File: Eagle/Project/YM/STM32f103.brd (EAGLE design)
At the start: 174.2 x 90.3 mm, 81 parts, among them IC1 YM3812, IC10 YM3812, IC11 YM3014B, IC12 LM358N, IC13 BA033CC0T, IC14 74ALS04N, IC15 6N136, IC2 YM3014B, IC3 LM358N, IC4 YM3812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

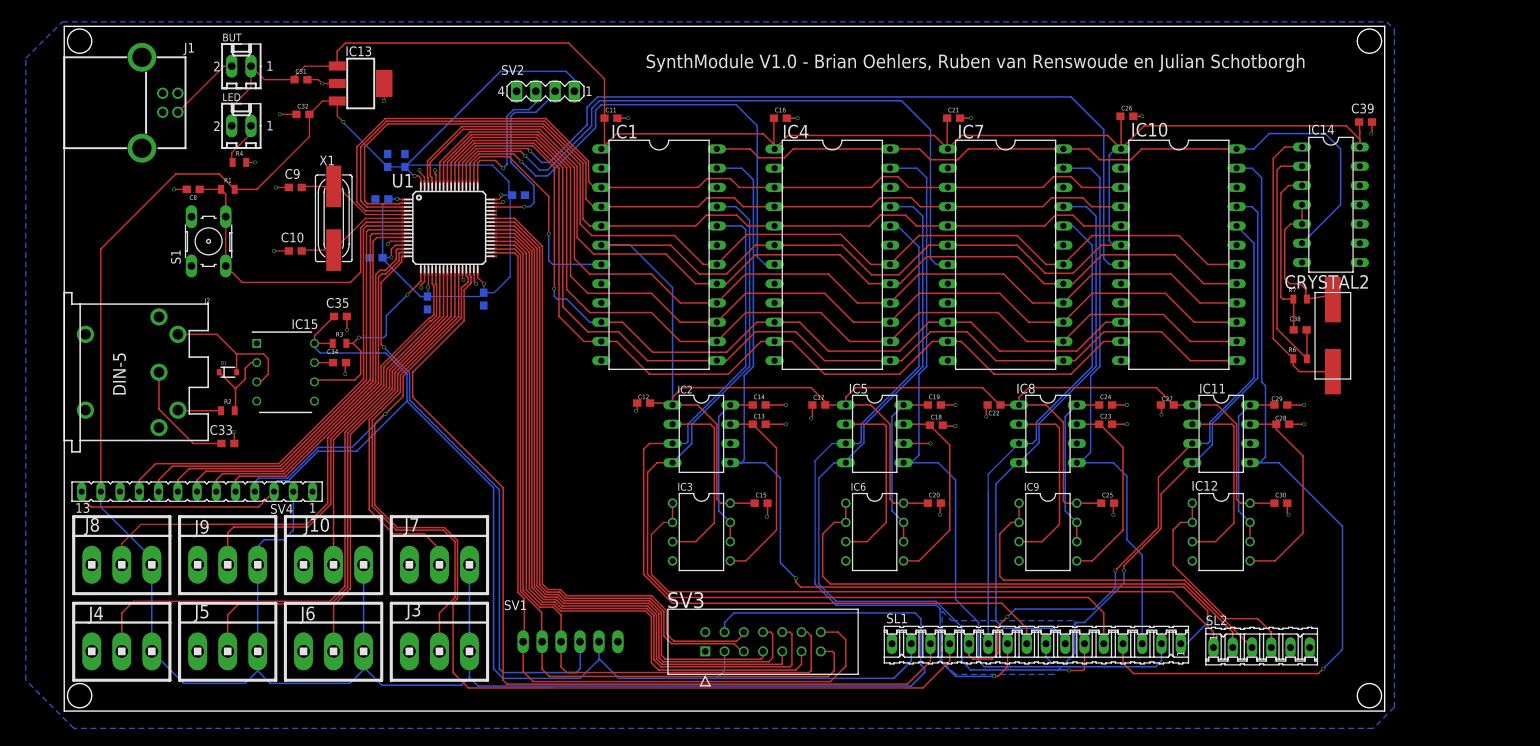
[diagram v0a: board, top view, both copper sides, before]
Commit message: PCB V5.0 LDO Adjustment
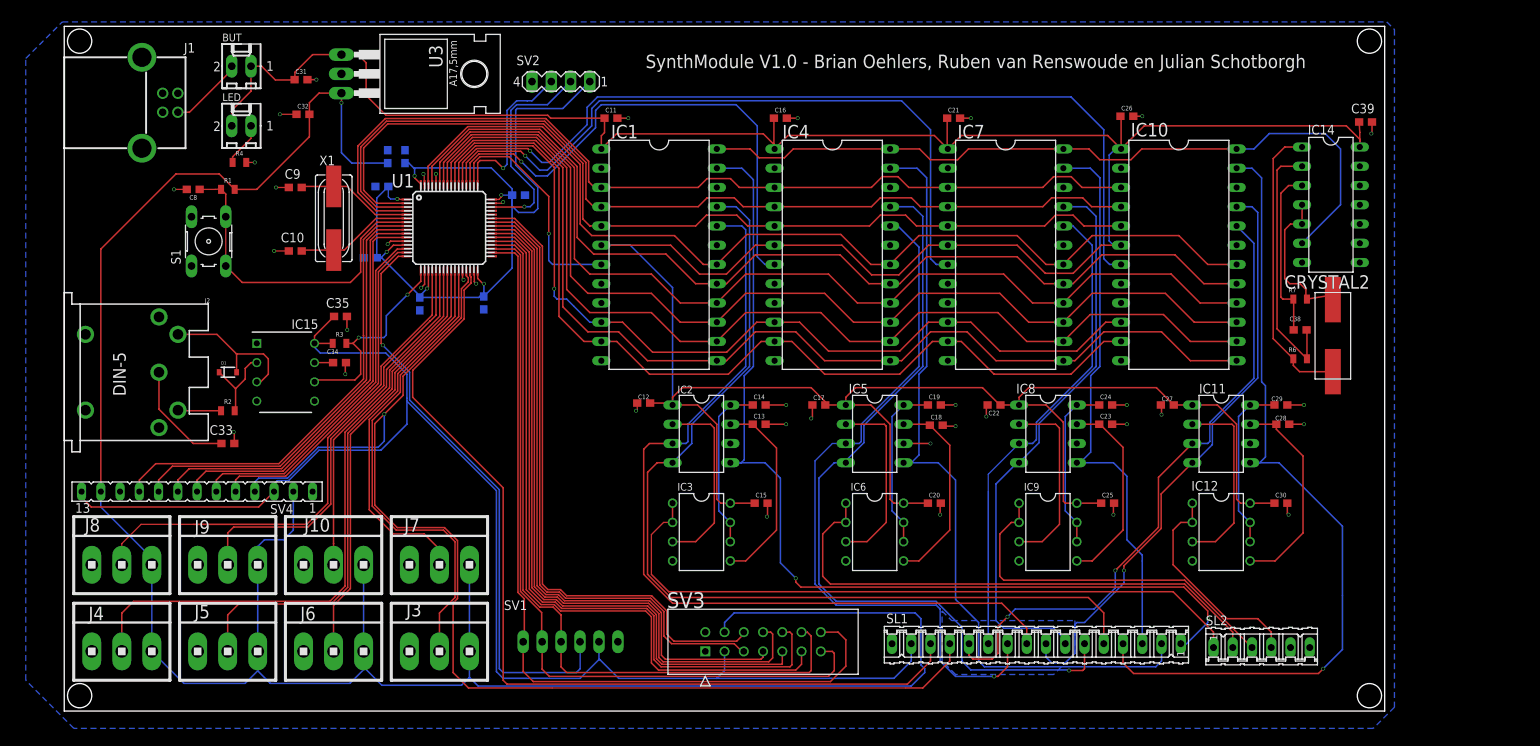
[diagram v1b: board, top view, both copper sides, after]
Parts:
- removed IC13: BA033CC0T, LDO:SOT223
- added U3: (no value), bt_regulator:TO220BH
- moved SV2 2.40 mm to (65.5, 83.1)
- moved C2 1.65 mm to (41.9, 69.2)
- moved C3 1.02 mm to (46.9, 53.7)
- moved C4 0.76 mm to (40.4, 59.8)
- moved C5 0.51 mm to (55.3, 53.8)
- moved C1 0.51 mm to (42.7, 73.2)
- moved C7 0.51 mm to (45.0, 73.2)
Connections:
- net 3.3V: now also U3.3; no longer IC13.3
- net 5V: now also U3.1; no longer IC13.1
- net GND: now also U3.2; no longer IC13.2, IC13.4
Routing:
- net 3.3V: track 417.2 -> 425.9 mm
- net GND: track 73.7 -> 67.3 mm, vias 39 -> 38
- net SW-DIO: track 25.8 -> 28.6 mm
- net SW-CLK: track 19.9 -> 22.0 mm
- net USART-TX-M4: track 159.1 -> 160.9 mm
- net YM-RST: track 125.3 -> 124.4 mm
- net RST: track 44.6 -> 43.8 mm
- net IO1: track 62.2 -> 61.4 mm
- net YM-A0: track 125.6 -> 124.8 mm
- net YM-WR: track 127.3 -> 126.6 mm
- net IO2: track 59.3 -> 58.6 mm
- net YM-D6: track 134.5 -> 133.8 mm
- net YM-D7: track 133.5 -> 133.0 mm

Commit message: V5.1 Connectors edit
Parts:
- removed SL1: (no value), con-amp-quick:16P
- removed SL2: (no value), con-amp-quick:06P
- added SV5: (no value), con-lsta:FE13
- added SV6: (no value), con-lsta:FE06
- moved R4 3.49 mm to (26.5, 73.0)
- moved J1 3.43 mm to (7.75, 76.8)
- moved C35 1.15 mm to (36.3, 50.9)
- moved C13 0.38 mm to (92.1, 37.8)
- moved U3 0.38 mm to (42.9, 84.5)
- moved C23 0.25 mm to (137.7, 37.8)
- moved C24 0.25 mm to (137.7, 40.4)
- moved C14 0.25 mm to (91.9, 40.4)
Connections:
- net 5V: now also SV5.12; no longer SL1.15
- net DAC-OUT-0: now also SV6.1; no longer SL2.1
- net DAC-OUT-1: now also SV6.2; no longer SL2.2
- net DAC-OUT-2: now also SV6.3; no longer SL2.3
- net DAC-OUT-3: now also SV6.4; no longer SL2.4
- net GND: now also SV5.13, SV6.6; no longer SL1.16, SL2.6
- net USART-RX-M4: now also SV5.11; no longer SL1.14
- net USART-TX-M4: now also SV5.10; no longer SL1.13
- net YM-CLK-I: now also SV5.1
- net YM1-CLK-O: no longer SL1.1
- net YM1-OUTPUT: now also SV5.2; no longer SL1.5
- net YM1-SYNC: now also SV5.6; no longer SL1.9
- net YM2-CLK-O: no longer SL1.2
- net YM2-OUTPUT: now also SV5.3; no longer SL1.6
- net YM2-SYNC: now also SV5.7; no longer SL1.10
- net YM3-CLK-O: no longer SL1.3
- net YM3-OUTPUT: now also SV5.4; no longer SL1.7
- net YM3-SYNC: now also SV5.8; no longer SL1.11
- net YM4-CLK-O: no longer SL1.4
- net YM4-OUTPUT: now also SV5.5; no longer SL1.8
- net YM4-SYNC: now also SV5.9; no longer SL1.12
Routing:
- net YM-CLK-I: track 101.9 -> 191.3 mm
- net YM1-CLK-O: track 129.1 -> 44.5 mm, vias 2 -> 0
- net YM4-CLK-O: track 108.5 -> 43.2 mm, vias 1 -> 0
- net YM2-CLK-O: track 104.8 -> 44.8 mm
- net 5V: track 664.9 -> 698.3 mm
- net YM3-CLK-O: track 74.7 -> 44.5 mm
- net YM4-OUTPUT: track 78.4 -> 84.3 mm, vias 1 -> 0
- net 3.3V: track 425.9 -> 421.3 mm
- net ADC-VOL3: track 56.6 -> 60.9 mm
- net 5VBUTTON: track 9.94 -> 14.2 mm
- net GND: track 67.3 -> 64.4 mm
- net YM4-SYNC: track 84.5 -> 86.5 mm, vias 2 -> 1
- net YM3-OUTPUT: track 74.5 -> 76.4 mm
- net DAC-OUT-1: track 71.0 -> 69.7 mm
- net N$13: track 5.99 -> 4.77 mm
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
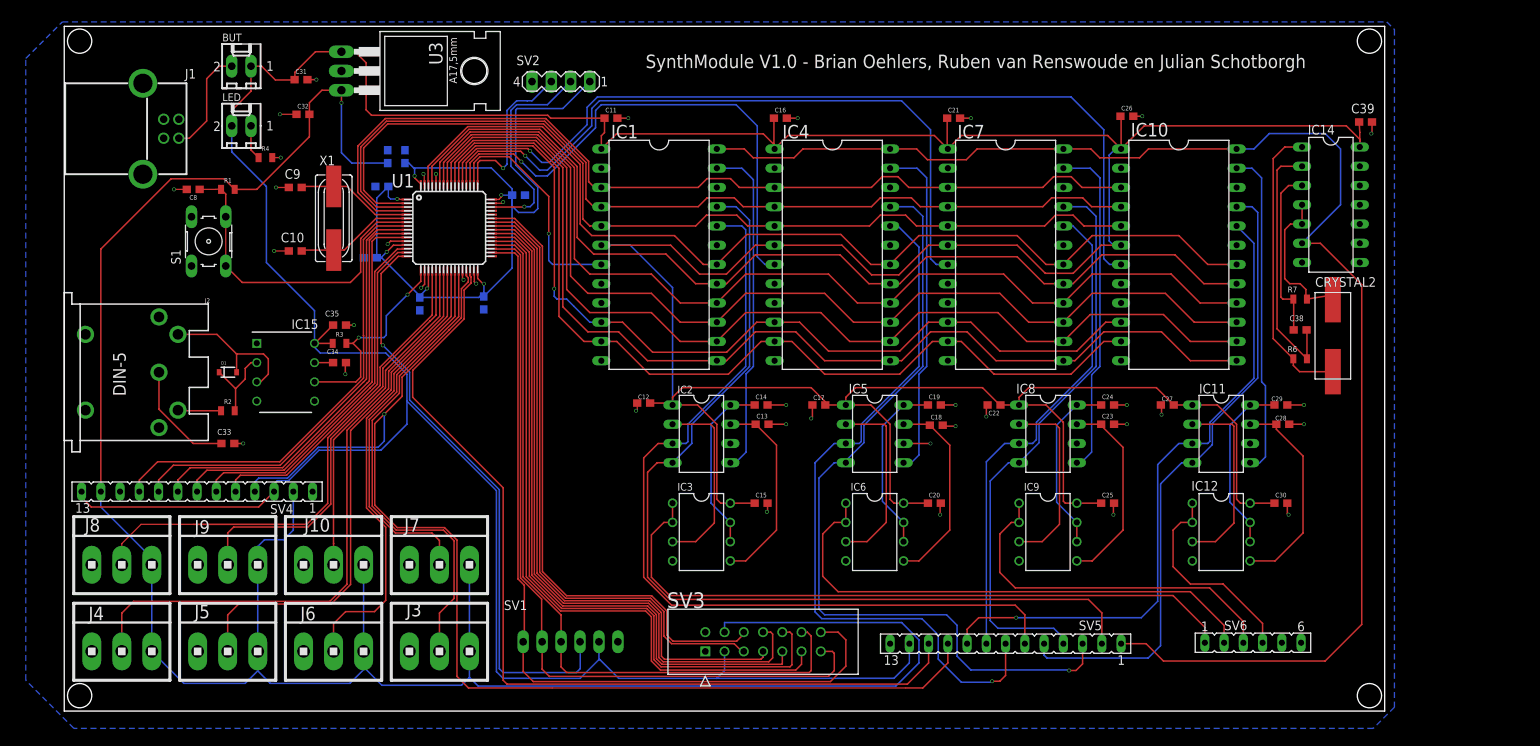
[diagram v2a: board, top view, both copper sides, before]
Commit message: Nieuwe versie - aanpassing aan: componenten, ground, namen van componenten, usb verschoven
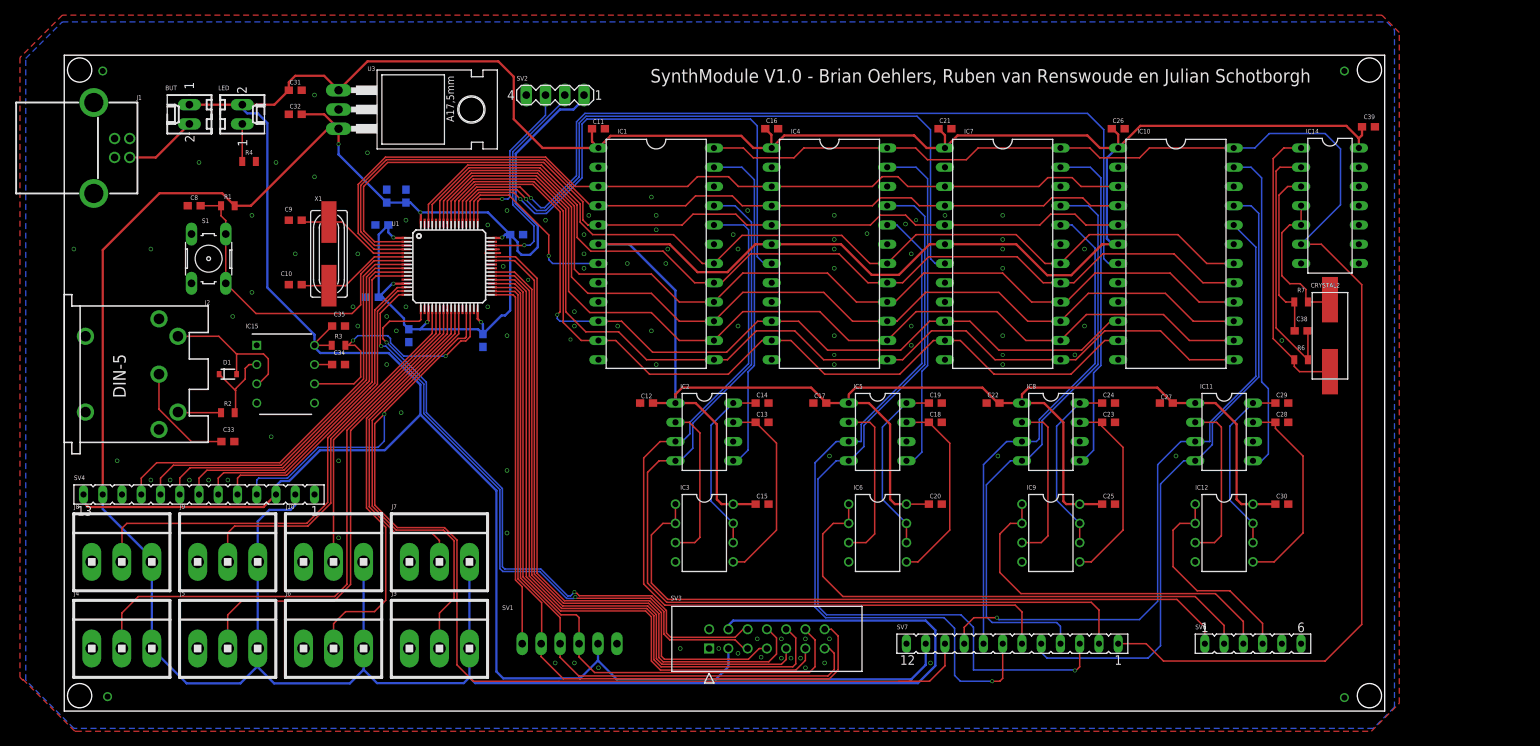
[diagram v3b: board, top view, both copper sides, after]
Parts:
- removed SV5: (no value), con-lsta:FE13
- added SV7: (no value), con-lsta:FE12
- C1, C2, C3, C5, C6: value 10nF -> 10n
- C10, C9: value 20pF -> 20p
- C11, C12, C15, C16, C17, C20, C21, C22, C25, C26, C27, C30, C8: value 100N -> 100n
- C13, C14, C18, C19, C23, C24, C28, C29: value 10UF -> 10u
- C31: value 0.47UF -> 0.47u
- C32: value 22UF -> 22u
- C33, C35, C39: value 100nF -> 100n
- C34: value 1p5F -> 1p5
- C38: value 4.7nF -> 4.7n
- C4: value 1uF -> 1u
- C7: value 4.7uF -> 4.7u
- IC12, IC3, IC6, IC9: value LM358N -> OPA2134
- moved BUT 9.35 mm to (16.5, 78.7), turned to 90 degrees
- moved J1 6.96 mm to (1.27, 74.3)
- moved C4 5.21 mm to (40.6, 54.6)
- moved C6 5.21 mm to (59.7, 62.9)
- moved C1 5.21 mm to (42.5, 67.9)
- moved C7 5.21 mm to (45.1, 67.9)
- moved U3 5.09 mm to (42.5, 79.4)
- moved C2 5.08 mm to (41.9, 64.1)
- moved U1 5.08 mm to (50.8, 58.7)
- moved C5 4.95 mm to (55.2, 48.9)
- moved X1 4.74 mm to (34.9, 60.3)
- moved C10 4.45 mm to (30.5, 56.3)
- moved C3 4.43 mm to (45.5, 49.5)
- moved C9 4.32 mm to (30.5, 64.8)
- moved S1 2.29 mm to (19.1, 59.7)
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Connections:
- removed net EXP1-INTA: SV3.8, U1.40
- removed net EXP1-INTB: SV3.7, U1.41
- removed net EXP2-INTA: SV3.5, U1.42
- removed net EXP2-INTB: SV3.6, U1.43
- removed net USART-RX-M4: SV5.11, U1.30
- new net EXP1-INT-A: SV3.8, U1.42
- new net EXP1-INT-B: SV3.7, U1.43
- new net EXP2-INT-A: SV3.5, U1.16
- new net EXP2-INT-B: SV3.6, U1.17
- net 5V: now also SV7.11; no longer SV5.12
- net EXP-SPI-CLK: now also SV1.2; no longer SV1.1
- net EXP-SPI-MISO: now also SV1.3; no longer SV1.2
- net EXP-SPI-MOSI: now also SV1.4; no longer SV1.3
- net GND: now also SV7.12, U1.40, U1.41, U1.44, U1.45; no longer SV5.13
- net LCD-SPI-CS: now also SV1.1, U1.33; no longer SV1.4, U1.16
- net USART-RX-MIDI: now also U1.30; no longer U1.17
- net USART-TX-M4: now also SV7.10; no longer SV5.10
- net YM-CLK-I: now also SV7.1; no longer SV5.1
- net YM1-OUTPUT: now also SV7.2; no longer SV5.2
- net YM1-SYNC: now also SV7.6; no longer SV5.6
- net YM2-OUTPUT: now also SV7.3; no longer SV5.3
- net YM2-SYNC: now also SV7.7; no longer SV5.7
- net YM3-OUTPUT: now also SV7.4; no longer SV5.4
- net YM3-SYNC: now also SV7.8; no longer SV5.8
- net YM4-OUTPUT: now also SV7.5; no longer SV5.5
- net YM4-SYNC: now also SV7.9; no longer SV5.9
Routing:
- net USART-RX-M4: track 122.2 -> 0.00 mm
- net EXP1-INTA: track 93.8 -> 0.00 mm
- net EXP1-INT-A: track 0.00 -> 89.8 mm
- net EXP1-INTB: track 88.7 -> 0.00 mm
- net EXP1-INT-B: track 0.00 -> 85.0 mm
- net EXP2-INT-A: track 0.00 -> 84.0 mm, vias 0 -> 2
- net EXP2-INTB: track 83.9 -> 0.00 mm
- net EXP2-INT-B: track 0.00 -> 83.7 mm, vias 0 -> 2
- net EXP2-INTA: track 83.6 -> 0.00 mm
- net GND: track 64.4 -> 6.10 mm, vias 38 -> 107
- net LCD-SPI-CS: track 77.5 -> 49.3 mm, vias 1 -> 0
- net EXP-SPI-CLK: track 109.9 -> 100.2 mm
- net USART-RX-MIDI: track 27.3 -> 35.3 mm
- net EXP-SPI-MISO: track 103.3 -> 95.4 mm
- net USART-TX-M4: track 160.3 -> 154.0 mm
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- added copper zone on layer 1, net GND
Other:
- board size 174.2 x 90.3 mm -> 174.2 x 86.5 mm

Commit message: verandere jumpers en verplaatsen din en usb.
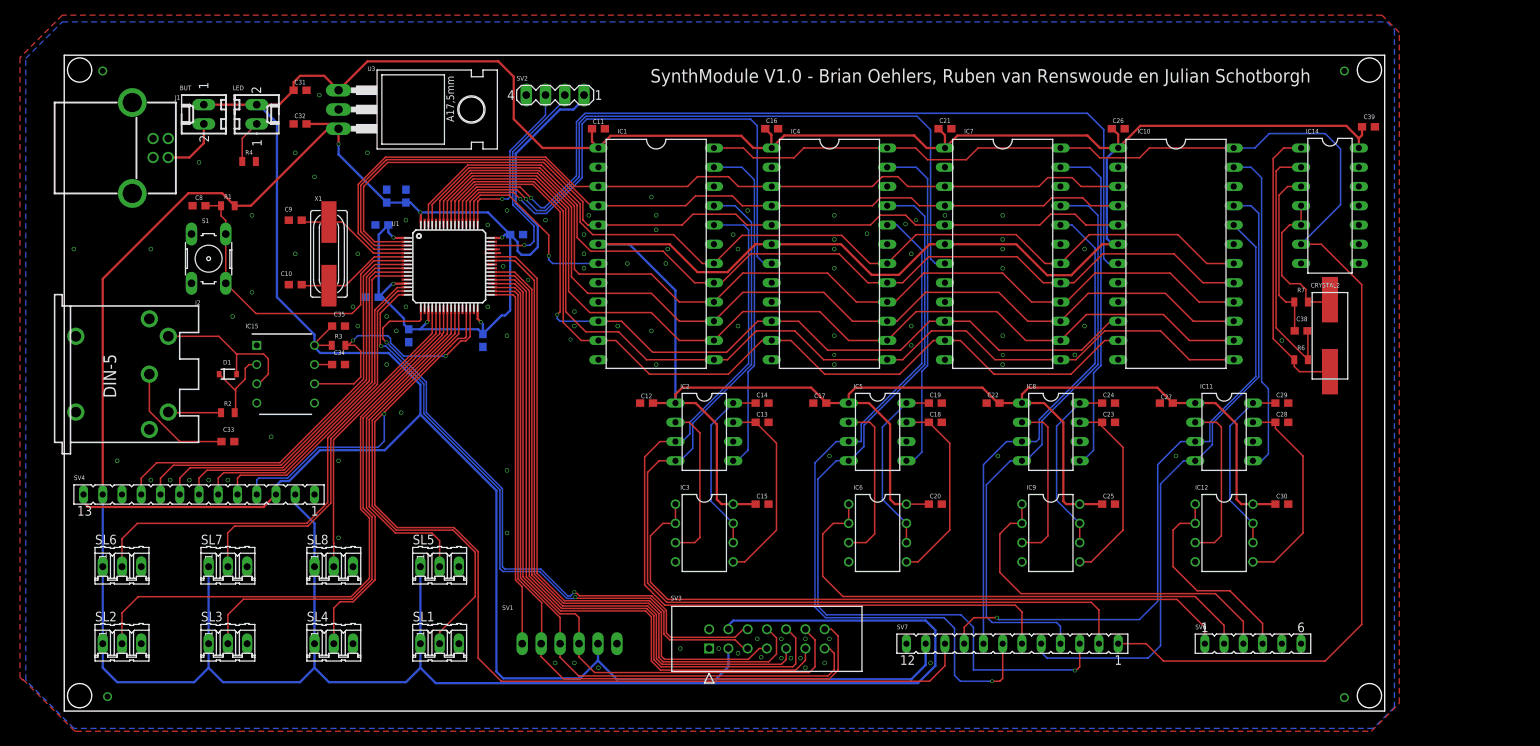
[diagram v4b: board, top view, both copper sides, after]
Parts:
- removed J10, J3, J4, J5, J6, J7, J8, J9: (no value), con-amp:1X3MTA
- added SL1, SL2, SL3, SL4, SL5, SL6, SL7, SL8: (no value), con-amp-quick:03P
- moved J1 5.08 mm to (6.35, 74.3)
- moved BUT 1.90 mm to (18.4, 78.7)
- moved LED 1.90 mm to (25.4, 78.7)
- moved C32 1.42 mm to (31.1, 77.5)
- moved J2 1.27 mm to (-1.27, 44.5)
- moved C8 0.64 mm to (17.8, 66.7)
- moved C31 0.63 mm to (31.1, 81.9)
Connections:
- net 3.3V: now also SL1.1, SL2.1, SL3.1, SL4.1, SL5.1, SL6.1, SL7.1, SL8.1; no longer J10.1, J3.1, J4.1, J5.1, J6.1, J7.1, J8.1, J9.1
- net ADC-VOL-TOT: now also SL1.2; no longer J3.2
- net ADC-VOL1: now also SL2.2; no longer J4.2
- net ADC-VOL2: now also SL3.2; no longer J5.2
- net ADC-VOL3: now also SL4.2; no longer J6.2
- net ADC-VOL4: now also SL5.2; no longer J7.2
- net ADC1: now also SL6.2; no longer J8.2
- net ADC2: now also SL7.2; no longer J9.2
- net ADC3: now also SL8.2; no longer J10.2
- net GND: now also SL1.3, SL2.3, SL3.3, SL4.3, SL5.3, SL6.3, SL7.3, SL8.3; no longer J10.3, J3.3, J4.3, J5.3, J6.3, J7.3, J8.3, J9.3
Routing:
- net 3.3V: track 425.0 -> 420.0 mm
- net 5V: track 696.0 -> 692.6 mm
- net ADC-VOL3: track 55.5 -> 52.5 mm
- net ADC-VOL-TOT: track 58.4 -> 60.8 mm
- net 5VBUTTON: track 9.70 -> 8.02 mm
- net ADC-VOL1: track 77.5 -> 79.1 mm
- net ADC-VOL2: track 63.9 -> 65.4 mm
- net N$18: track 14.6 -> 16.1 mm
- net N$19: track 5.72 -> 6.99 mm
- net N$16: track 19.9 -> 21.2 mm
- net USART-TX-M4: track 154.0 -> 152.8 mm
- net N$13: track 4.96 -> 5.75 mm
- net ADC3: track 39.1 -> 39.7 mm
- net ADC2: track 50.4 -> 51.0 mm
- net ADC-VOL4: track 44.6 -> 45.3 mm
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
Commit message: update lcd header
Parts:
- removed SV1: (no value), con-amp-mt:S06P
- added SL9: (no value), con-amp-quick:06P
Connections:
- net 5V: now also SL9.5; no longer SV1.5
- net EXP-SPI-CLK: now also SL9.2; no longer SV1.2
- net EXP-SPI-MISO: now also SL9.3; no longer SV1.3
- net EXP-SPI-MOSI: now also SL9.4; no longer SV1.4
- net GND: now also SL9.6; no longer SV1.6
- net LCD-SPI-CS: now also SL9.1; no longer SV1.1
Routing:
- net 5V: track 692.6 -> 693.4 mm
- net LCD-SPI-CS: track 49.3 -> 48.6 mm
- net GND: track 6.10 -> 5.46 mm
